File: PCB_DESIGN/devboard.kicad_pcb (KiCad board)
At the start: 2 copper layers, 32 parts, among them J1 USB_C_Receptacle_USB2.0_14P, J2 Conn_02x18_Odd_Even, J3 Conn_02x18_Odd_Even, SW1 SW_Push, U1 RP2040, U2 NCP1117-3.3_SOT223, U3 W25Q128JVS, Y1 12 MHz

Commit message: fixed all images finally with new schematic
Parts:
- added J4: Conn_01x03, Connector_PinHeader_2.54mm:PinHeader_1x03_P2.54mm_Vertical, F.Cu at (52.7, 21.6)
- J2, J3: value Conn_02x18_Odd_Even -> Conn_01x20; footprint Connector_PinHeader_2.54mm:PinHeader_2x18_P2.54mm_Vertical -> Connector_PinHeader_2.54mm:PinHeader_1x20_P2.54mm_Vertical
- moved J2 12.1 mm to (43.6, 21.6)
- moved J3 11.4 mm to (48.1, 21.6)
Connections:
- J2 pad 1: GND -> GPIO0
- J2 pad 10: GPIO3 -> GPIO7
- J2 pad 11: GND -> GPIO8
- J2 pad 12: GPIO4 -> GPIO9
- J2 pad 14: GPIO5 -> GPIO10
- J2 pad 15: GND -> GPIO11
- J2 pad 16: GPIO6 -> GPIO12
- J2 pad 17: GND -> GPIO13
- J2 pad 18: GPIO7 -> GND
- J2 pad 19: GND -> GPIO14
- J2 pad 2: +3V3 -> GPIO1
- J2 pad 20: GPIO8 -> GPIO15
- J2 pad 4: GPIO0 -> GPIO2
- J2 pad 5: GND -> GPIO3
- J2 pad 6: GPIO1 -> GPIO4
- J2 pad 7: GND -> GPIO5
- J2 pad 8: GPIO2 -> GND
- J2 pad 9: GND -> GPIO6
- J3 pad 1: GPIO29_ADC3 -> VBUS
- J3 pad 10: GND -> GPIO23
- J3 pad 11: GPIO24 -> RUN
- J3 pad 12: GND -> GPIO22
- J3 pad 13: GPIO23 -> GND
- J3 pad 14: GND -> GPIO21
- J3 pad 15: GPIO22 -> GPIO20
- J3 pad 16: GND -> GPIO19
- J3 pad 17: GPIO21 -> GPIO18
- J3 pad 19: GPIO20 -> GPIO17
- J3 pad 2: GND -> GPIO29_ADC3
- J3 pad 20: GND -> GPIO16
- J3 pad 3: GPIO28_ADC2 -> GND
- J3 pad 4: GND -> GPIO28_ADC2
- J3 pad 5: GPIO27_ADC1 -> +3V3
- J3 pad 6: GND -> GPIO27_ADC1
- J3 pad 9: GPIO25 -> GPIO24
- U1 pad 37: GPIO25 -> unconnected-(U1-GPIO25-Pad37)

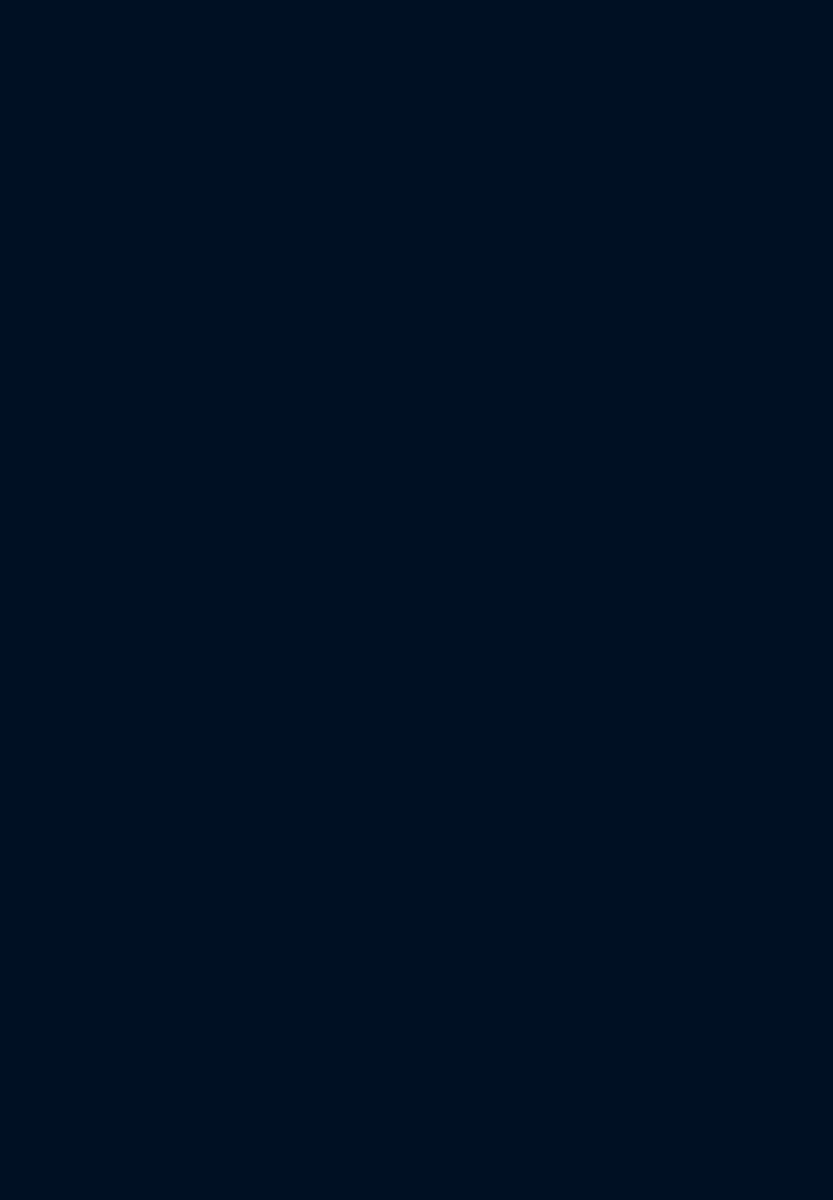
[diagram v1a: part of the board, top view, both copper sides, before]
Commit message: mounting holes and outline
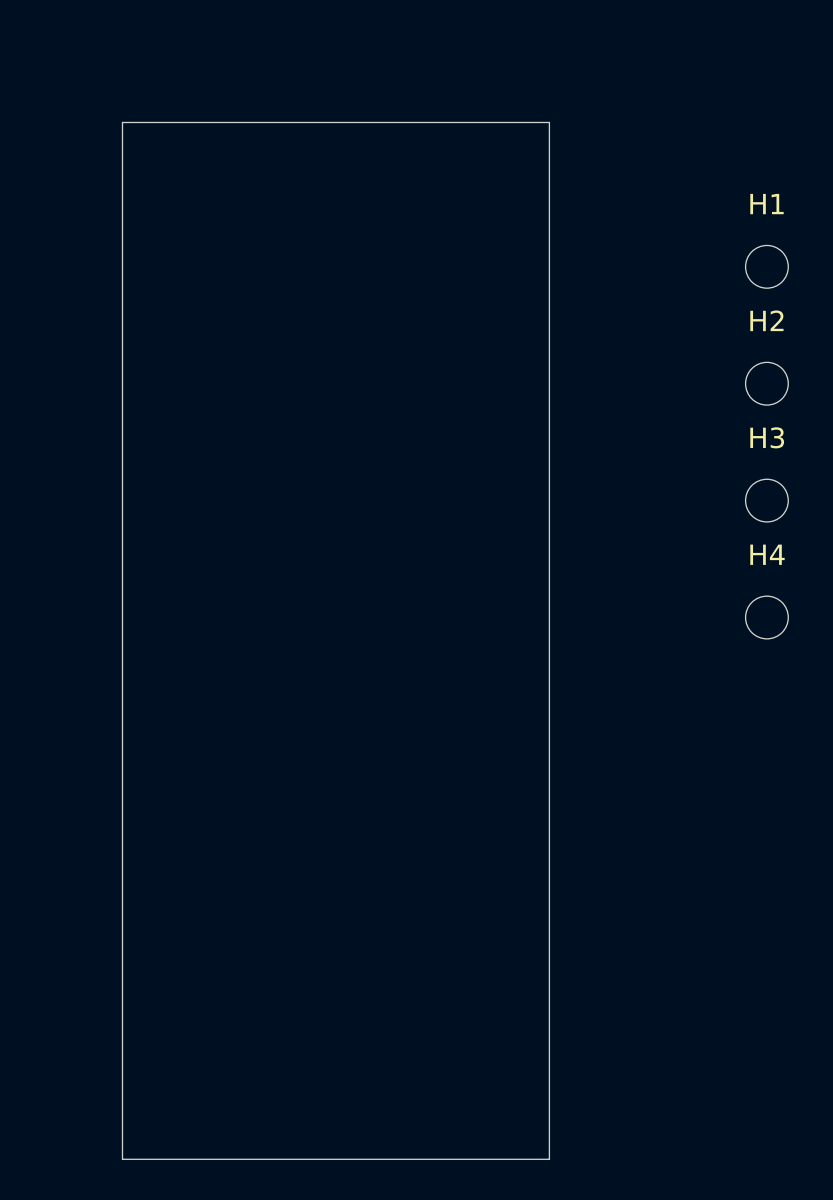
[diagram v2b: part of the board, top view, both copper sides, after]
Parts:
- added H1: MountingHole, MountingHole:MountingHole_2.1mm, F.Cu at (181.8, 53.9)
- added H2: MountingHole, MountingHole:MountingHole_2.1mm, F.Cu at (181.8, 59.6)
- added H3: MountingHole, MountingHole:MountingHole_2.1mm, F.Cu at (181.8, 65.3)
- added H4: MountingHole, MountingHole:MountingHole_2.1mm, F.Cu at (181.8, 71.1)
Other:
- board outline added: 21 x 51 mm

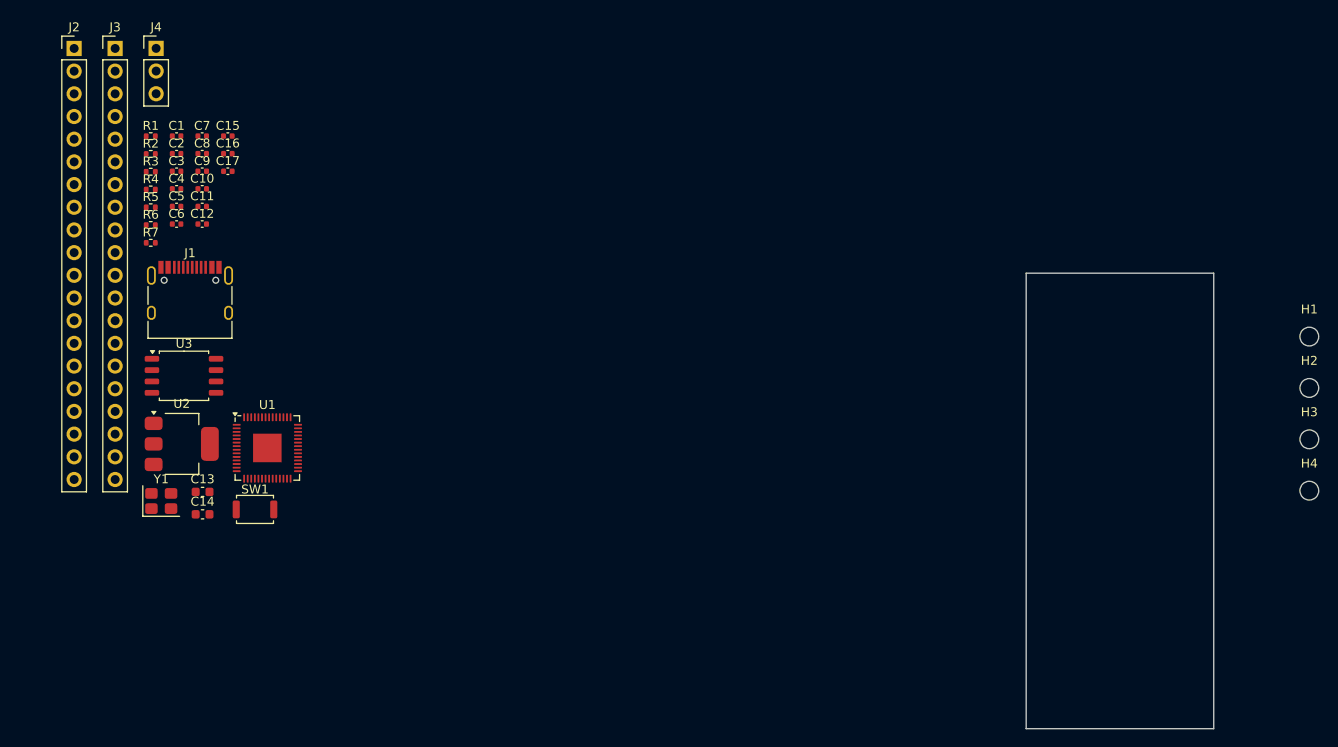
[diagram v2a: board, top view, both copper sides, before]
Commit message: removing mounting holes, not enough space
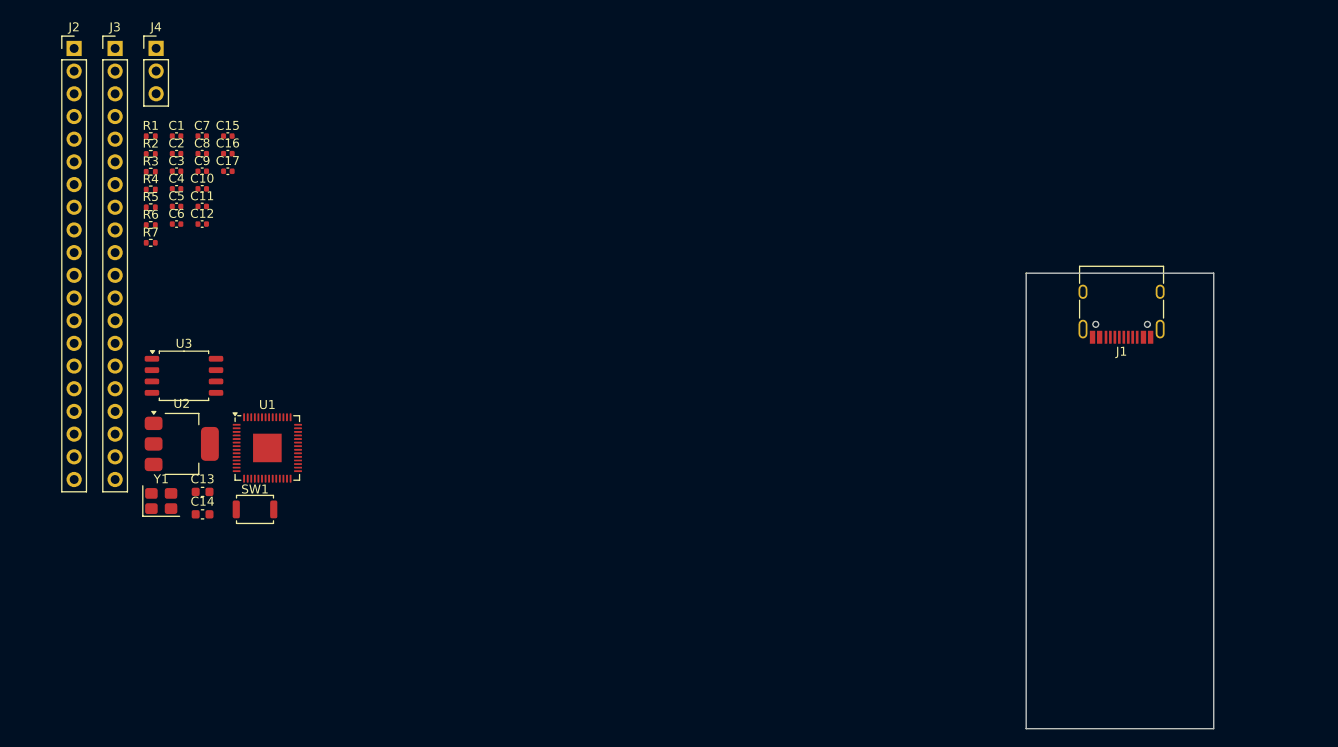
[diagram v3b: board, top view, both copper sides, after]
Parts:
- removed H1, H2, H3, H4: MountingHole, MountingHole:MountingHole_2.1mm
- moved J1 104.3 mm to (160.8, 49.9), turned to 180 degrees

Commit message: aligning USB-C and SoC
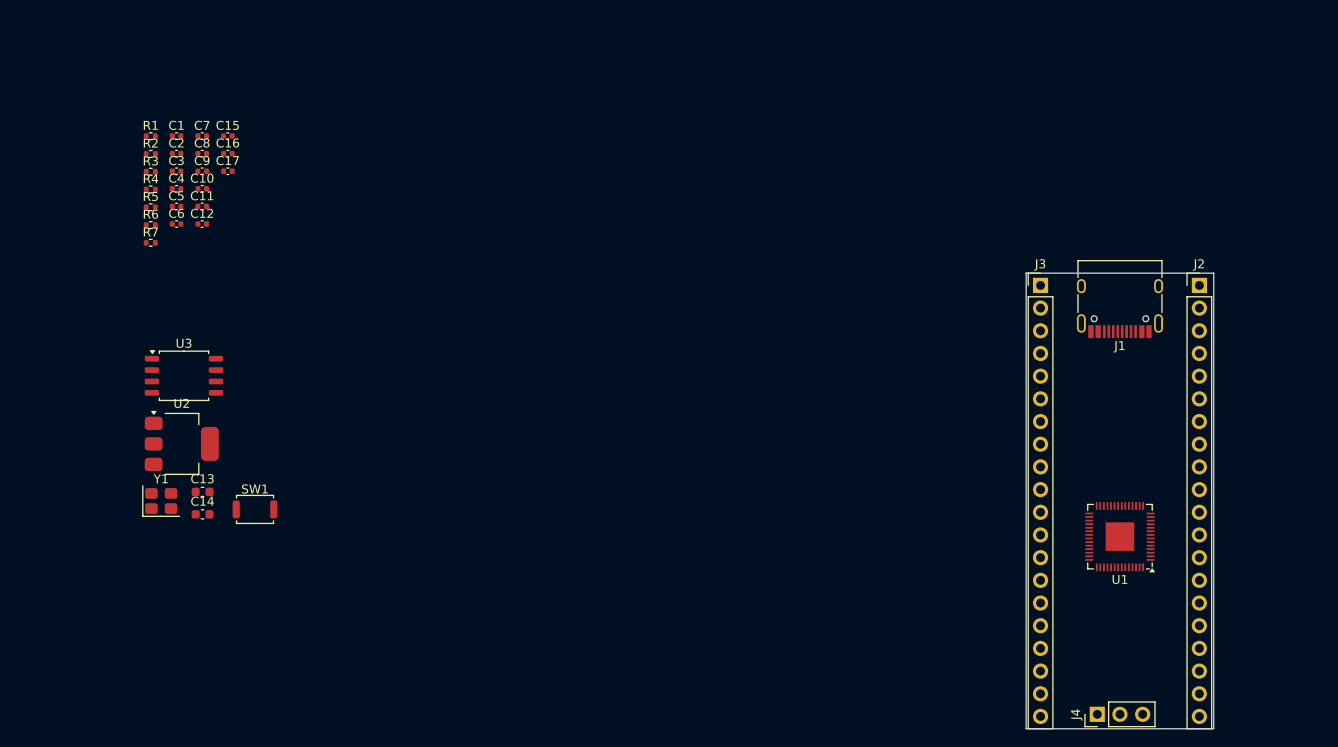
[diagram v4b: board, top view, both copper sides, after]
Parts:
- moved J4 129.1 mm to (158.1, 96.1), turned to 90 degrees
- moved J2 128.7 mm to (169.5, 48.1)
- moved J3 107.0 mm to (151.8, 48.1)
- moved U1 96.0 mm to (160.7, 76.2), turned to 180 degrees
- moved J1 0.66 mm to (160.7, 49.2)

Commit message: fixed LDO and flash memory, did lots of layout stuff
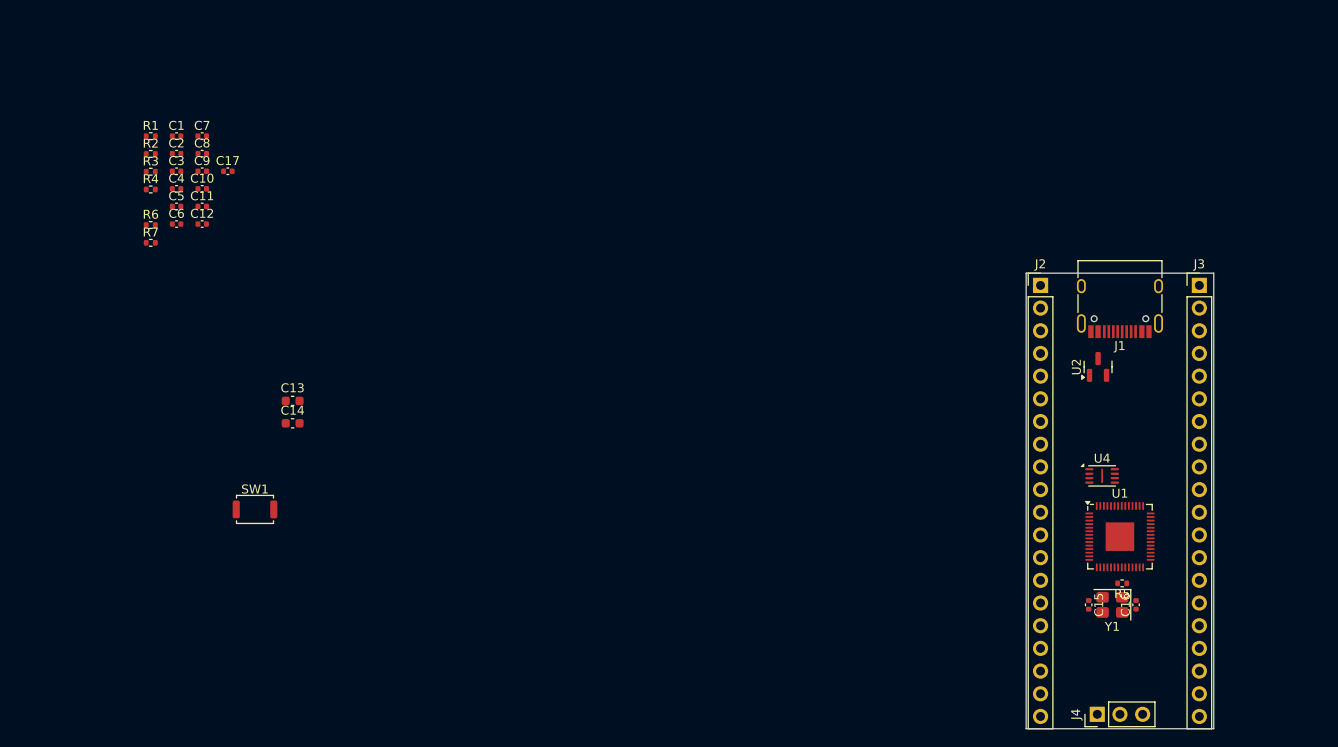
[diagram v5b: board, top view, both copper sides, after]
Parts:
- removed U3: W25Q128JVS, Package_SO:SOIC-8_5.3x5.3mm_P1.27mm
- added U4: W25Q16JVUXIQ TR, Package_SON:Winbond_USON-8-1EP_3x2mm_P0.5mm_EP0.2x1.6mm, F.Cu at (158.7, 69.5)
- U2: value NCP1117-3.3_SOT223 -> MCP1700x-330xxTT; footprint Package_TO_SOT_SMD:SOT-223-3_TabPin2 -> Package_TO_SOT_SMD:SOT-23
- moved R5 116.6 mm to (160.9, 81.5), turned to 180 degrees
- moved C16 113.5 mm to (162.4, 83.9), turned to 90 degrees
- moved C15 109.7 mm to (157.2, 83.9), turned to -90 degrees
- moved Y1 107.1 mm to (159.8, 83.9), turned to 180 degrees
- moved U2 103.0 mm to (158.2, 57.2), turned to 90 degrees
- moved J2 17.8 mm to (151.8, 48.1)
- moved J3 17.8 mm to (169.5, 48.1)
- moved C13 14.3 mm to (68.0, 61.0)
- moved C14 14.3 mm to (68.0, 63.6)
- turned U1 to 0 degrees

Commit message: added all the decoupling capacitors
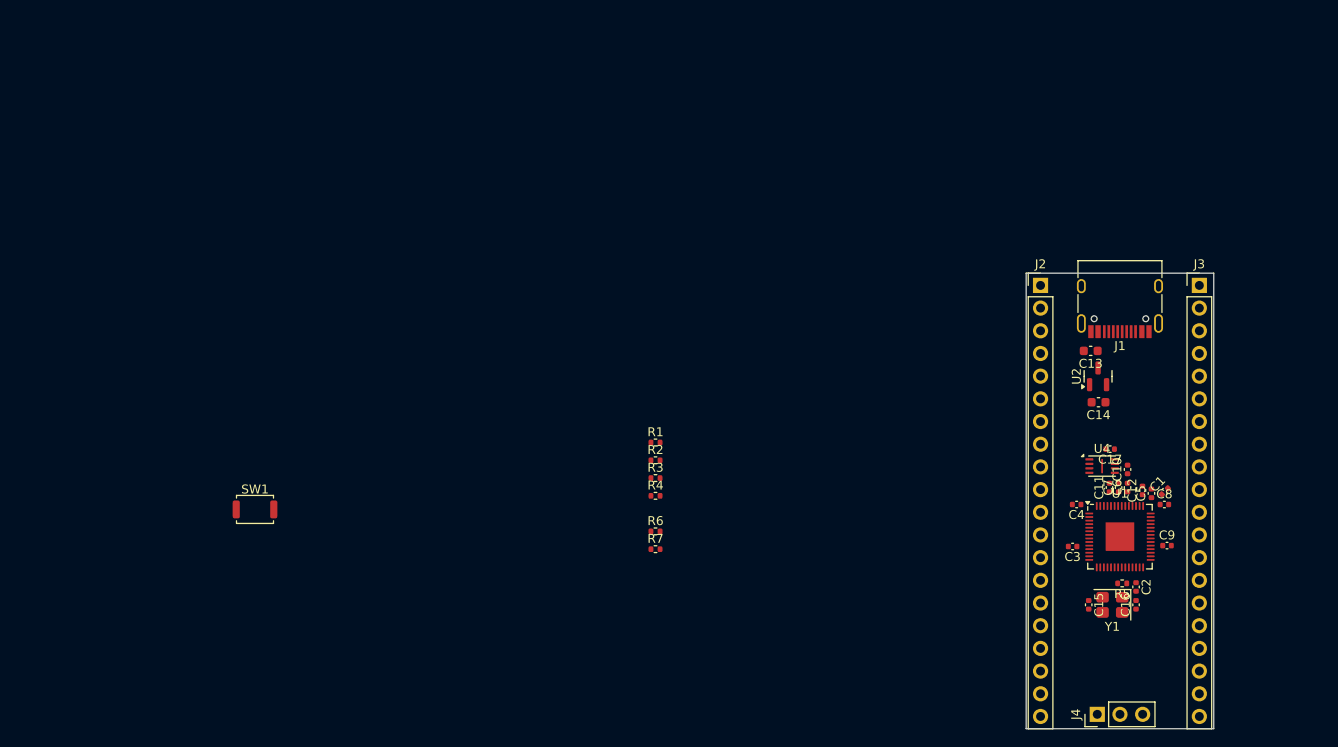
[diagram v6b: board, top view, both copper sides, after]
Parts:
- moved C2 117.9 mm to (162.4, 81.9), turned to -90 degrees
- moved C1 117.6 mm to (165.7, 71.2), turned to 45 degrees
- moved C9 115.9 mm to (165.9, 77.2)
- moved C8 114.7 mm to (165.6, 72.7)
- moved C5 113.8 mm to (164.2, 71.4), turned to 90 degrees
- moved C6 110.5 mm to (161.5, 70.8), turned to 90 degrees
- moved C7 109.9 mm to (160.5, 70.8), turned to 90 degrees
- moved C12 109.4 mm to (163.2, 71.1), turned to 90 degrees
- moved C3 108.8 mm to (155.3, 77.3), turned to 180 degrees
- moved C10 108.3 mm to (161.5, 68.7), turned to 90 degrees
- moved C4 106.8 mm to (155.8, 72.7), turned to 180 degrees
- moved C11 106.3 mm to (159.5, 70.8), turned to 90 degrees
- moved C17 103.6 mm to (159.6, 66.5), turned to 180 degrees
- moved C14 90.3 mm to (158.2, 61.2), turned to 180 degrees
- moved C13 89.5 mm to (157.4, 55.5), turned to 180 degrees
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
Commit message: starting to route
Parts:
- moved C10 27.0 mm to (135.6, 61.2)
- moved C6 27.0 mm to (135.6, 63.2)
- moved C7 27.0 mm to (134.6, 63.2)
- moved C11 27.0 mm to (133.6, 63.2)
- moved R4 11.6 mm to (115.6, 62.5)
- moved R3 11.6 mm to (115.6, 60.5)
- moved C17 1.26 mm to (158.3, 66.6)
- moved U4 1.22 mm to (157.4, 68.6)
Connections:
- net USB_D+ renamed /USB_DP
- net USB_D- renamed /USB_DN
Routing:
- net QSPI_SS: track 0.00 -> 7.16 mm
- net QSPI_SD1: track 0.00 -> 6.71 mm
- net QSPI_SD2: track 0.00 -> 5.43 mm
- net QSPI_SD3: track 0.00 -> 5.41 mm
- net QSPI_SCLK: track 0.00 -> 4.58 mm
- net QSPI_SD0: track 0.00 -> 3.64 mm
